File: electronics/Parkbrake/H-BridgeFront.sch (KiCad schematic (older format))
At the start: 82 parts

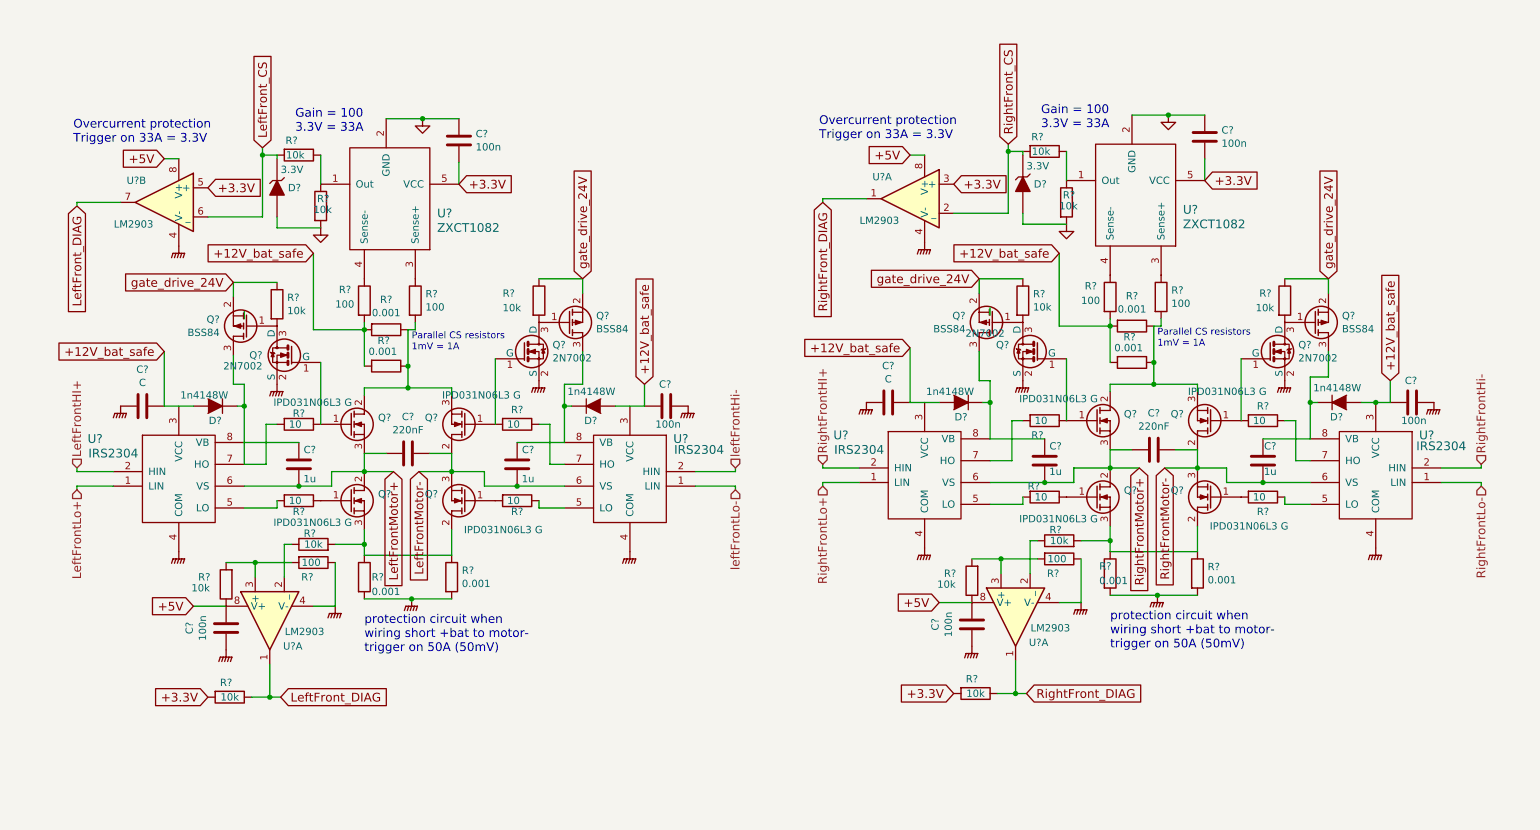
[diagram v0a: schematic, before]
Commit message: Fixes to Bat switch and polarity protection
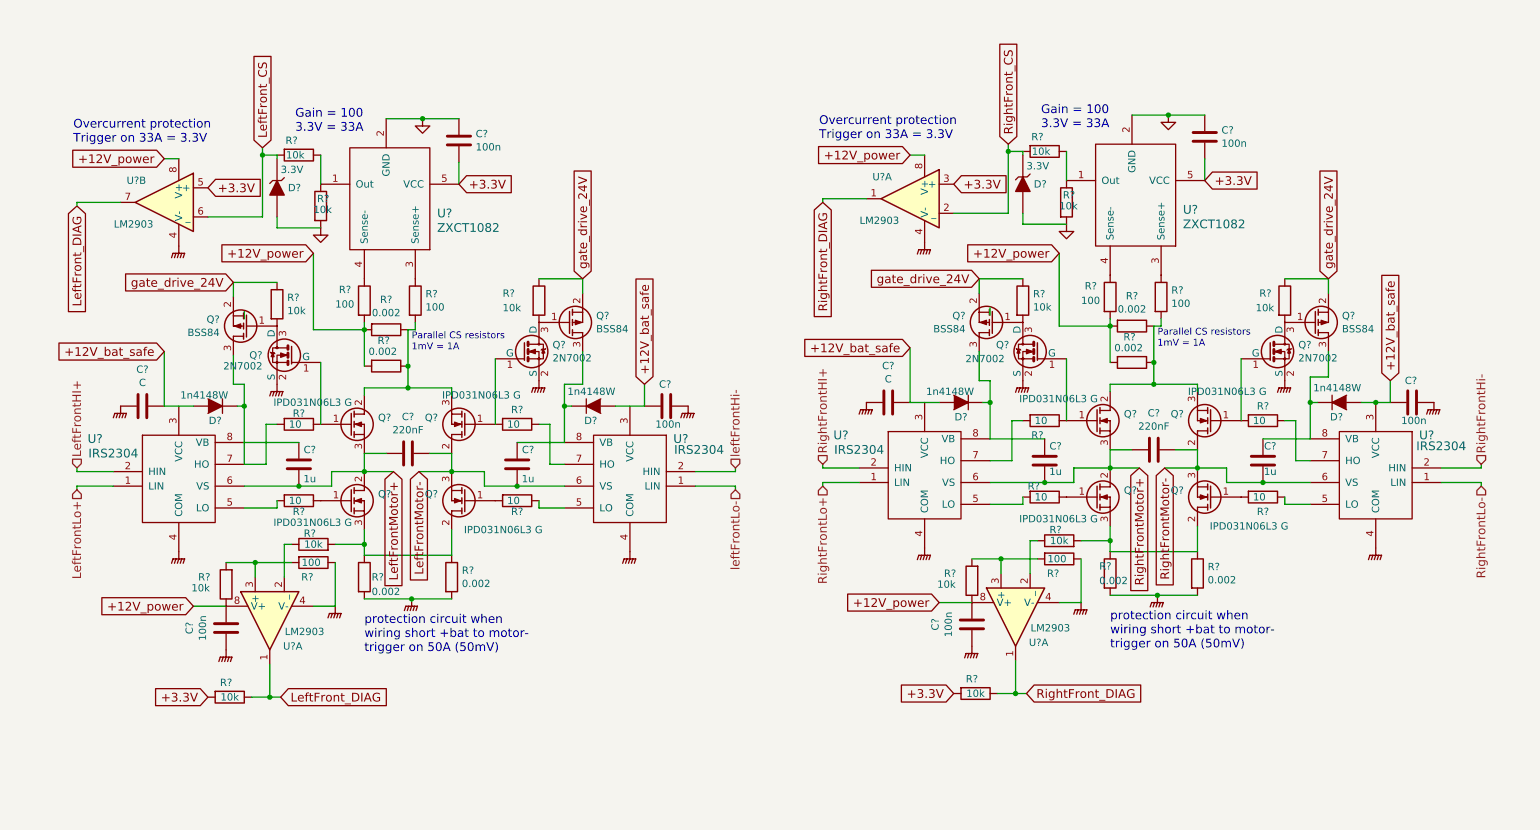
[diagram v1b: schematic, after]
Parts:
- R? (x8): value 0.001 -> 0.002
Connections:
- net +12V_bat_safe: no longer R?.2, R?.2, R?.2, R?.2, R?.2, R?.2
- net +5V renamed +12V_power
- net +12V_power: now also R?.2, R?.2, R?.2, R?.2, R?.2, R?.2
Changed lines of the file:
@@
 P 2850 4700
 F 0 "R?" H 2900 4700 50  0000 L CNN
-F 1 "0.001" H 2900 4600 50  0000 L CNN
+F 1 "0.002" H 2900 4600 50  0000 L CNN
 F 2 "Resistors_SMD:R_2512_HandSoldering" H 2920 4609 50  0001 L CNN
 F 3 "" H 2850 4700 50  0000 C CNN
@@
 P 3450 4700
 F 0 "R?" H 3520 4746 50  0000 L CNN
-F 1 "0.001" H 3520 4655 50  0000 L CNN
+F 1 "0.002" H 3520 4655 50  0000 L CNN
 F 2 "Resistors_SMD:R_2512_HandSoldering" H 3520 4609 50  0001 L CNN
 F 3 "" H 3450 4700 50  0000 C CNN
@@
 P 3000 3000
 F 0 "R?" V 2793 3000 50  0000 C CNN
-F 1 "0.001" V 2884 3000 50  0000 C CNN
+F 1 "0.002" V 2884 3000 50  0000 C CNN
 F 2 "Resistors_SMD:R_2512_HandSoldering" H 3070 2909 50  0001 L CNN
 F 3 "" H 3000 3000 50  0000 C CNN
@@
 P 3000 3250
 F 0 "R?" V 2825 3275 50  0000 R CNN
-F 1 "0.001" V 2900 3325 50  0000 R CNN
+F 1 "0.002" V 2900 3325 50  0000 R CNN
 F 2 "Resistors_SMD:R_2512_HandSoldering" H 3070 3159 50  0001 L CNN
 F 3 "" H 3000 3250 50  0000 C CNN
@@
 $EndComp
 Text GLabel 2500 2475 0    60   Input ~ 0
-+12V_bat_safe
++12V_power
 $Comp
 L C C?
@@
 	2250 1800 2250 1825
 Text GLabel 1475 1825 0    60   Input ~ 0
-+5V
++12V_power
 Wire Wire Line
 	1575 1825 1475 1825
@@
 	875  2125 875  2150
 Text GLabel 1675 4900 0    60   Input ~ 0
-+5V
++12V_power
 Text GLabel 1775 2025 2    60   Input ~ 0
 +3.3V
@@
 P 7975 4675
 F 0 "R?" H 7900 4725 50  0000 L CNN
-F 1 "0.001" H 7900 4625 50  0000 L CNN
+F 1 "0.002" H 7900 4625 50  0000 L CNN
 F 2 "Resistors_SMD:R_2512_HandSoldering" H 8045 4584 50  0001 L CNN
 F 3 "" H 7975 4675 50  0000 C CNN
@@
 P 8575 4675
 F 0 "R?" H 8645 4721 50  0000 L CNN
-F 1 "0.001" H 8645 4630 50  0000 L CNN
+F 1 "0.002" H 8645 4630 50  0000 L CNN
 F 2 "Resistors_SMD:R_2512_HandSoldering" H 8645 4584 50  0001 L CNN
 F 3 "" H 8575 4675 50  0000 C CNN
@@
 P 8125 2975
 F 0 "R?" V 7918 2975 50  0000 C CNN
-F 1 "0.001" V 8009 2975 50  0000 C CNN
+F 1 "0.002" V 8009 2975 50  0000 C CNN
 F 2 "Resistors_SMD:R_2512_HandSoldering" H 8195 2884 50  0001 L CNN
 F 3 "" H 8125 2975 50  0000 C CNN
@@
 P 8125 3225
 F 0 "R?" V 7950 3250 50  0000 R CNN
-F 1 "0.001" V 8025 3300 50  0000 R CNN
+F 1 "0.002" V 8025 3300 50  0000 R CNN
 F 2 "Resistors_SMD:R_2512_HandSoldering" H 8195 3134 50  0001 L CNN
 F 3 "" H 8125 3225 50  0000 C CNN
@@
 $EndComp
 Text GLabel 7625 2475 0    60   Input ~ 0
-+12V_bat_safe
++12V_power
 $Comp
 L C C?
@@
 P 7475 3150
 F 0 "Q?" H 7669 3196 50  0000 L CNN
-F 1 "2N7002" H 7700 3275 50  0000 L CNN
+F 1 "2N7002" H 7700 3100 50  0000 L CNN
 F 2 "TO_SOT_Packages_SMD:SOT-23_Handsoldering" H 7668 3059 50  0001 L CIN
 F 3 "" H 7475 3150 50  0000 L CNN
@@
 	7375 1775 7375 1800
 Text GLabel 6600 1800 0    60   Input ~ 0
-+5V
++12V_power
 Wire Wire Line
 	6700 1800 6600 1800
@@
 	6000 2100 6000 2125
 Text GLabel 6800 4875 0    60   Input ~ 0
-+5V
++12V_power
 Text GLabel 6900 2000 2    60   Input ~ 0
 +3.3V

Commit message: Add currentlimit latching to avaoid current limit oscilation Start a mcu schema part
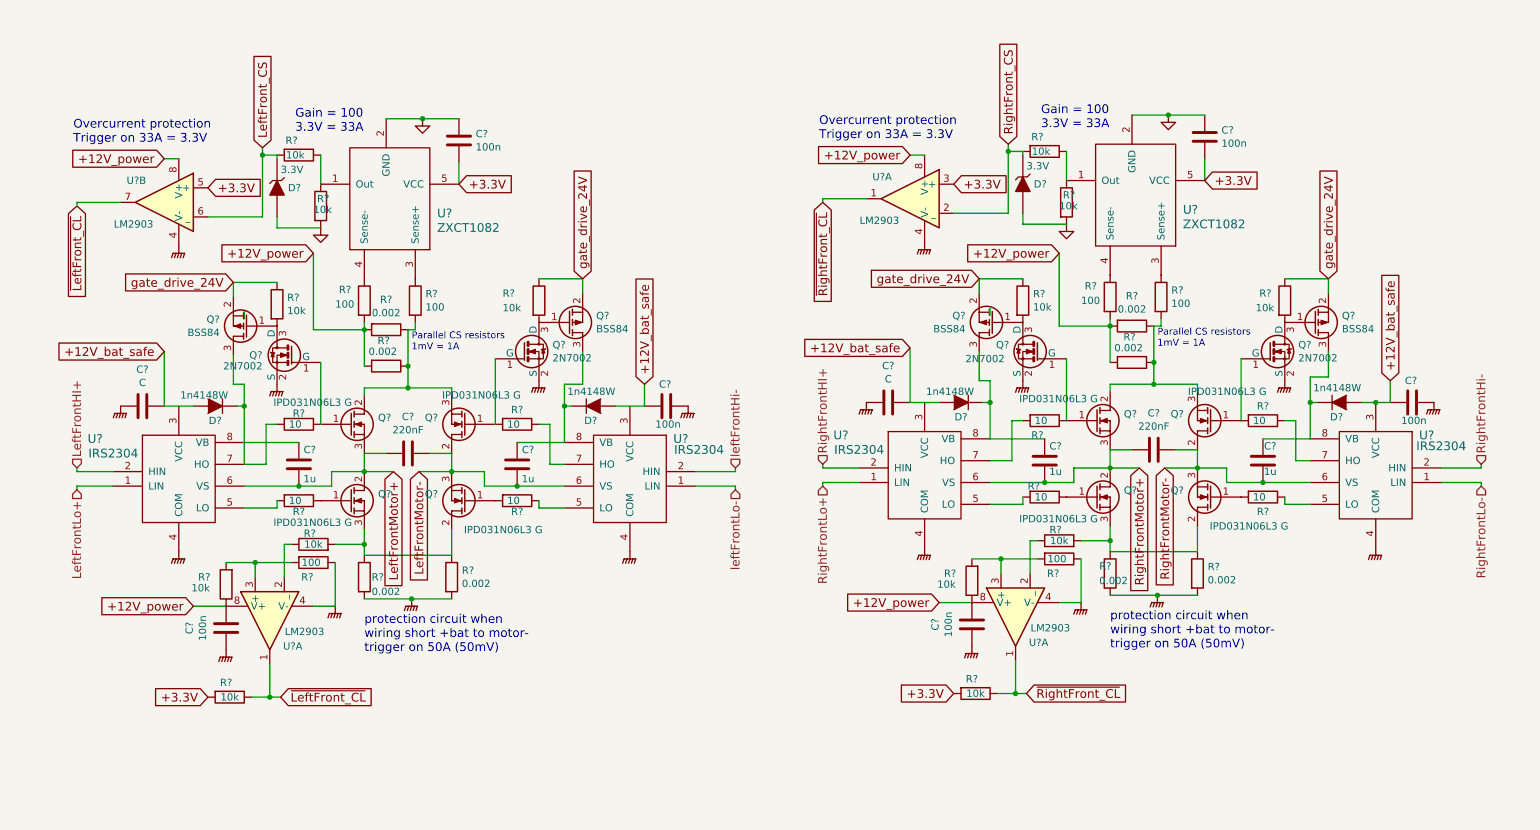
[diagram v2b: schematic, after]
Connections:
- net LeftFront_DIAG renamed ~LeftFront_CL
- net RightFront_DIAG renamed ~RightFront_CL
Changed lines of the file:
@@
 $Descr A4 11693 8268
 encoding utf-8
-Sheet 4 5
+Sheet 4 6
 Title ""
 Date ""
@@
 	4050 4225 4050 4175
 Text GLabel 2275 5525 2    60   Input ~ 0
-LeftFront_DIAG
+~LeftFront_CL
 Text GLabel 3050 3975 3    60   Input ~ 0
 LeftFrontMotor+
@@
 LeftFrontMotor-
 Text GLabel 875  2150 3    60   Input ~ 0
-LeftFront_DIAG
+~LeftFront_CL
 Text GLabel 7400 5500 2    60   Input ~ 0
-RightFront_DIAG
+~RightFront_CL
 Text GLabel 6000 2125 3    60   Input ~ 0
-RightFront_DIAG
+~RightFront_CL
 Text GLabel 8175 3950 3    60   Input ~ 0
 RightFrontMotor+

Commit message: More work on parkbrake node
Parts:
- R? (x3): footprint (none) -> Resistors_SMD:R_0805; farnell (none) -> MC01W08051100R; part (none) -> 9332375
- R?: footprint (none) -> Resistors_SMD:R_0805; farnell (none) -> 9332375; part (none) -> MC01W08051100R
- R? (x13): footprint (none) -> Resistors_SMD:R_0805; farnell (none) -> 9332391; part (none) -> MC01W0805110K
- R? (x8): footprint (none) -> Resistors_SMD:R_1206; farnell (none) -> 9335790; part (none) -> MC0125W1206110R
- R?: footprint (none) -> Resistors_SMD:R_0805; part (none) -> MC01W0805110K
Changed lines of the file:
@@
 LIBS:teensy
 LIBS:power_switches
+LIBS:stm32
 LIBS:Parkbrake-cache
 EELAYER 25 0
@@
 $Descr A4 11693 8268
 encoding utf-8
-Sheet 4 6
+Sheet 4 10
 Title ""
 Date ""
@@
 F 0 "R?" H 3270 2846 50  0000 L CNN
 F 1 "100" H 3270 2755 50  0000 L CNN
-F 2 "" V 3130 2800 50  0000 C CNN
+F 2 "Resistors_SMD:R_0805" V 3130 2800 50  0001 C CNN
 F 3 "" H 3200 2800 50  0000 C CNN
+F 4 "9332375" H 3200 2800 60  0001 C CNN "part"
+F 5 "MC01W08051100R" H 3200 2800 60  0001 C CNN "farnell"
 	1    3200 2800
 	1    0    0    -1
@@
 F 0 "R?" H 2675 2875 50  0000 L CNN
 F 1 "100" H 2650 2775 50  0000 L CNN
-F 2 "" V 2780 2800 50  0000 C CNN
+F 2 "Resistors_SMD:R_0805" V 2780 2800 50  0001 C CNN
 F 3 "" H 2850 2800 50  0000 C CNN
+F 4 "9332375" H 2850 2800 60  0001 C CNN "farnell"
+F 5 "MC01W08051100R" H 2850 2800 60  0001 C CNN "part"
 	1    2850 2800
 	1    0    0    -1
@@
 F 0 "R?" H 2525 2200 50  0000 L CNN
 F 1 "10k" H 2500 2125 50  0000 L CNN
-F 2 "" V 2480 2150 50  0000 C CNN
+F 2 "Resistors_SMD:R_0805" V 2480 2150 50  0001 C CNN
 F 3 "" H 2550 2150 50  0000 C CNN
+F 4 "MC01W0805110K" H 2550 2150 60  0001 C CNN "part"
+F 5 "9332391" H 2550 2150 60  0001 C CNN "farnell"
 	1    2550 2150
 	1    0    0    -1
@@
 F 0 "R?" V 3975 4175 50  0000 C CNN
 F 1 "10" V 3900 4150 50  0000 C CNN
-F 2 "" V 3830 4175 50  0000 C CNN
+F 2 "Resistors_SMD:R_1206" V 3830 4175 50  0001 C CNN
 F 3 "" H 3900 4175 50  0000 C CNN
+F 4 "9335790" V 3900 4175 60  0001 C CNN "farnell"
+F 5 "MC0125W1206110R" V 3900 4175 60  0001 C CNN "part"
 	1    3900 4175
 	0    1    1    0
@@
 F 0 "R?" V 2475 4175 50  0000 C CNN
 F 1 "10" V 2400 4150 50  0000 C CNN
-F 2 "" V 2330 4175 50  0000 C CNN
+F 2 "Resistors_SMD:R_1206" V 2330 4175 50  0001 C CNN
 F 3 "" H 2400 4175 50  0000 C CNN
+F 4 "9335790" V 2400 4175 60  0001 C CNN "farnell"
+F 5 "MC0125W1206110R" V 2400 4175 60  0001 C CNN "part"
 	1    2400 4175
 	0    1    1    0
@@
 F 0 "R?" V 2325 3650 50  0000 C CNN
 F 1 "10" V 2400 3625 50  0000 C CNN
-F 2 "" V 2330 3650 50  0000 C CNN
+F 2 "Resistors_SMD:R_1206" V 2330 3650 50  0001 C CNN
 F 3 "" H 2400 3650 50  0000 C CNN
+F 4 "MC0125W1206110R" V 2400 3650 60  0001 C CNN "part"
+F 5 "9335790" V 2400 3650 60  0001 C CNN "farnell"
 	1    2400 3650
 	0    1    1    0
@@
 F 0 "R?" V 3800 3650 50  0000 C CNN
 F 1 "10" V 3900 3625 50  0000 C CNN
-F 2 "" V 3830 3650 50  0000 C CNN
+F 2 "Resistors_SMD:R_1206" V 3830 3650 50  0001 C CNN
 F 3 "" H 3900 3650 50  0000 C CNN
+F 4 "9335790" V 3900 3650 60  0001 C CNN "farnell"
+F 5 "MC0125W1206110R" V 3900 3650 60  0001 C CNN "part"
 	1    3900 3650
 	0    1    1    0
@@
 F 0 "R?" H 2050 4700 50  0000 C CNN
 F 1 "10k" H 2075 4775 50  0000 C CNN
-F 2 "" V 1830 4750 50  0000 C CNN
+F 2 "Resistors_SMD:R_0805" V 1830 4750 50  0001 C CNN
 F 3 "" H 1900 4750 50  0000 C CNN
+F 4 "MC01W0805110K" H 1900 4750 60  0001 C CNN "part"
+F 5 "9332391" H 1900 4750 60  0001 C CNN "farnell"
 	1    1900 4750
 	-1   0    0    1
@@
 F 0 "R?" V 2575 4500 50  0000 C CNN
 F 1 "10k" V 2500 4475 50  0000 C CNN
-F 2 "" V 2430 4475 50  0000 C CNN
+F 2 "Resistors_SMD:R_0805" V 2430 4475 50  0001 C CNN
 F 3 "" H 2500 4475 50  0000 C CNN
+F 4 "MC01W0805110K" V 2500 4475 60  0001 C CNN "part"
+F 5 "9332391" V 2500 4475 60  0001 C CNN "farnell"
 	1    2500 4475
 	0    -1   -1   0
@@
 F 0 "R?" V 1825 5500 50  0000 C CNN
 F 1 "10k" V 1925 5525 50  0000 C CNN
-F 2 "" V 1855 5525 50  0000 C CNN
+F 2 "Resistors_SMD:R_0805" V 1855 5525 50  0001 C CNN
 F 3 "" H 1925 5525 50  0000 C CNN
+F 4 "MC01W0805110K" V 1925 5525 60  0001 C CNN "part"
+F 5 "9332391" V 1925 5525 60  0001 C CNN "farnell"
 	1    1925 5525
 	0    1    1    0
@@
 F 0 "R?" V 2300 1750 50  0000 C CNN
 F 1 "10k" V 2400 1775 50  0000 C CNN
-F 2 "" V 2330 1800 50  0000 C CNN
+F 2 "Resistors_SMD:R_0805" V 2330 1800 50  0001 C CNN
 F 3 "" H 2400 1800 50  0000 C CNN
+F 4 "MC01W0805110K" V 2400 1800 60  0001 C CNN "part"
+F 5 "9332391" V 2400 1800 60  0001 C CNN "farnell"
 	1    2400 1800
 	0    1    1    0
@@
 F 0 "R?" H 8395 2821 50  0000 L CNN
 F 1 "100" H 8395 2730 50  0000 L CNN
-F 2 "" V 8255 2775 50  0000 C CNN
+F 2 "Resistors_SMD:R_0805" V 8255 2775 50  0001 C CNN
 F 3 "" H 8325 2775 50  0000 C CNN
+F 4 "9332375" H 8325 2775 60  0001 C CNN "part"
+F 5 "MC01W08051100R" H 8325 2775 60  0001 C CNN "farnell"
 	1    8325 2775
 	1    0    0    -1
@@
 F 0 "R?" H 7800 2850 50  0000 L CNN
 F 1 "100" H 7775 2750 50  0000 L CNN
-F 2 "" V 7905 2775 50  0000 C CNN
+F 2 "Resistors_SMD:R_0805" V 7905 2775 50  0001 C CNN
 F 3 "" H 7975 2775 50  0000 C CNN
+F 4 "9332375" H 7975 2775 60  0001 C CNN "part"
+F 5 "MC01W08051100R" H 7975 2775 60  0001 C CNN "farnell"
 	1    7975 2775
 	1    0    0    -1
@@
 F 0 "R?" H 7650 2175 50  0000 L CNN
 F 1 "10k" H 7625 2100 50  0000 L CNN
-F 2 "" V 7605 2125 50  0000 C CNN
+F 2 "Resistors_SMD:R_0805" V 7605 2125 50  0001 C CNN
 F 3 "" H 7675 2125 50  0000 C CNN
+F 4 "MC01W0805110K" H 7675 2125 60  0001 C CNN "part"
 	1    7675 2125
 	1    0    0    -1
@@
 F 0 "R?" V 9125 4150 50  0000 C CNN
 F 1 "10" V 9025 4125 50  0000 C CNN
-F 2 "" V 8955 4150 50  0000 C CNN
+F 2 "Resistors_SMD:R_1206" V 8955 4150 50  0001 C CNN
 F 3 "" H 9025 4150 50  0000 C CNN
+F 4 "9335790" V 9025 4150 60  0001 C CNN "farnell"
+F 5 "MC0125W1206110R" V 9025 4150 60  0001 C CNN "part"
 	1    9025 4150
 	0    1    1    0
@@
 F 0 "R?" V 7450 4075 50  0000 C CNN
 F 1 "10" V 7525 4125 50  0000 C CNN
-F 2 "" V 7455 4150 50  0000 C CNN
+F 2 "Resistors_SMD:R_1206" V 7455 4150 50  0001 C CNN
 F 3 "" H 7525 4150 50  0000 C CNN
+F 4 "9335790" V 7525 4150 60  0001 C CNN "farnell"
+F 5 "MC0125W1206110R" V 7525 4150 60  0001 C CNN "part"
 	1    7525 4150
 	0    1    1    0
@@
 F 0 "R?" V 7625 3575 50  0000 C CNN
 F 1 "10" V 7525 3600 50  0000 C CNN
-F 2 "" V 7455 3625 50  0000 C CNN
+F 2 "Resistors_SMD:R_1206" V 7455 3625 50  0001 C CNN
 F 3 "" H 7525 3625 50  0000 C CNN
+F 4 "9335790" V 7525 3625 60  0001 C CNN "farnell"
+F 5 "MC0125W1206110R" V 7525 3625 60  0001 C CNN "part"
 	1    7525 3625
 	0    1    1    0
@@
 F 0 "R?" V 8925 3625 50  0000 C CNN
 F 1 "10" V 9025 3600 50  0000 C CNN
-F 2 "" V 8955 3625 50  0000 C CNN
+F 2 "Resistors_SMD:R_1206" V 8955 3625 50  0001 C CNN
 F 3 "" H 9025 3625 50  0000 C CNN
+F 4 "9335790" V 9025 3625 60  0001 C CNN "farnell"
+F 5 "MC0125W1206110R" V 9025 3625 60  0001 C CNN "part"
 	1    9025 3625
 	0    1    1    0
@@
 F 0 "R?" H 7175 4675 50  0000 C CNN
 F 1 "10k" H 7200 4750 50  0000 C CNN
-F 2 "" V 6955 4725 50  0000 C CNN
+F 2 "Resistors_SMD:R_0805" V 6955 4725 50  0001 C CNN
 F 3 "" H 7025 4725 50  0000 C CNN
+F 4 "MC01W0805110K" H 7025 4725 60  0001 C CNN "part"
+F 5 "9332391" H 7025 4725 60  0001 C CNN "farnell"
 	1    7025 4725
 	-1   0    0    1
@@
 F 0 "R?" V 7700 4475 50  0000 C CNN
 F 1 "10k" V 7625 4450 50  0000 C CNN
-F 2 "" V 7555 4450 50  0000 C CNN
+F 2 "Resistors_SMD:R_0805" V 7555 4450 50  0001 C CNN
 F 3 "" H 7625 4450 50  0000 C CNN
+F 4 "MC01W0805110K" V 7625 4450 60  0001 C CNN "part"
+F 5 "9332391" V 7625 4450 60  0001 C CNN "farnell"
 	1    7625 4450
 	0    -1   -1   0
@@
 F 0 "R?" V 6950 5475 50  0000 C CNN
 F 1 "10k" V 7050 5500 50  0000 C CNN
-F 2 "" V 6980 5500 50  0000 C CNN
+F 2 "Resistors_SMD:R_0805" V 6980 5500 50  0001 C CNN
 F 3 "" H 7050 5500 50  0000 C CNN
+F 4 "MC01W0805110K" V 7050 5500 60  0001 C CNN "part"
+F 5 "9332391" V 7050 5500 60  0001 C CNN "farnell"
 	1    7050 5500
 	0    1    1    0
@@
 F 0 "R?" V 7425 1725 50  0000 C CNN
 F 1 "10k" V 7525 1750 50  0000 C CNN
-F 2 "" V 7455 1775 50  0000 C CNN
+F 2 "Resistors_SMD:R_0805" V 7455 1775 50  0001 C CNN
 F 3 "" H 7525 1775 50  0000 C CNN
+F 4 "MC01W0805110K" V 7525 1775 60  0001 C CNN "part"
+F 5 "9332391" V 7525 1775 60  0001 C CNN "farnell"
 	1    7525 1775
 	0    1    1    0
@@
 F 0 "R?" H 3800 2850 50  0000 L CNN
 F 1 "10k" H 3800 2750 50  0000 L CNN
-F 2 "" V 3980 2800 50  0000 C CNN
+F 2 "Resistors_SMD:R_0805" V 3980 2800 50  0001 C CNN
 F 3 "" H 4050 2800 50  0000 C CNN
+F 4 "MC01W0805110K" H 4050 2800 60  0001 C CNN "part"
+F 5 "9332391" H 4050 2800 60  0001 C CNN "farnell"
 	1    4050 2800
 	1    0    0    -1
@@
 F 0 "R?" H 2320 2871 50  0000 L CNN
 F 1 "10k" H 2320 2780 50  0000 L CNN
-F 2 "" V 2180 2825 50  0000 C CNN
+F 2 "Resistors_SMD:R_0805" V 2180 2825 50  0001 C CNN
 F 3 "" H 2250 2825 50  0000 C CNN
+F 4 "MC01W0805110K" H 2250 2825 60  0001 C CNN "part"
+F 5 "9332391" H 2250 2825 60  0001 C CNN "farnell"
 	1    2250 2825
 	1    0    0    -1
@@
 F 0 "R?" H 9000 2850 50  0000 L CNN
 F 1 "10k" H 8975 2750 50  0000 L CNN
-F 2 "" V 9105 2800 50  0000 C CNN
+F 2 "Resistors_SMD:R_0805" V 9105 2800 50  0001 C CNN
 F 3 "" H 9175 2800 50  0000 C CNN
+F 4 "MC01W0805110K" H 9175 2800 60  0001 C CNN "part"
+F 5 "9332391" H 9175 2800 60  0001 C CNN "farnell"
 	1    9175 2800
 	1    0    0    -1
@@
 F 0 "R?" H 7445 2846 50  0000 L CNN
 F 1 "10k" H 7445 2755 50  0000 L CNN
-F 2 "" V 7305 2800 50  0000 C CNN
+F 2 "Resistors_SMD:R_0805" V 7305 2800 50  0001 C CNN
 F 3 "" H 7375 2800 50  0000 C CNN
+F 4 "MC01W0805110K" H 7375 2800 60  0001 C CNN "part"
+F 5 "9332391" H 7375 2800 60  0001 C CNN "farnell"
 	1    7375 2800
 	1    0    0    -1
